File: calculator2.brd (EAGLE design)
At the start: 72.8 x 140 mm, 41 parts

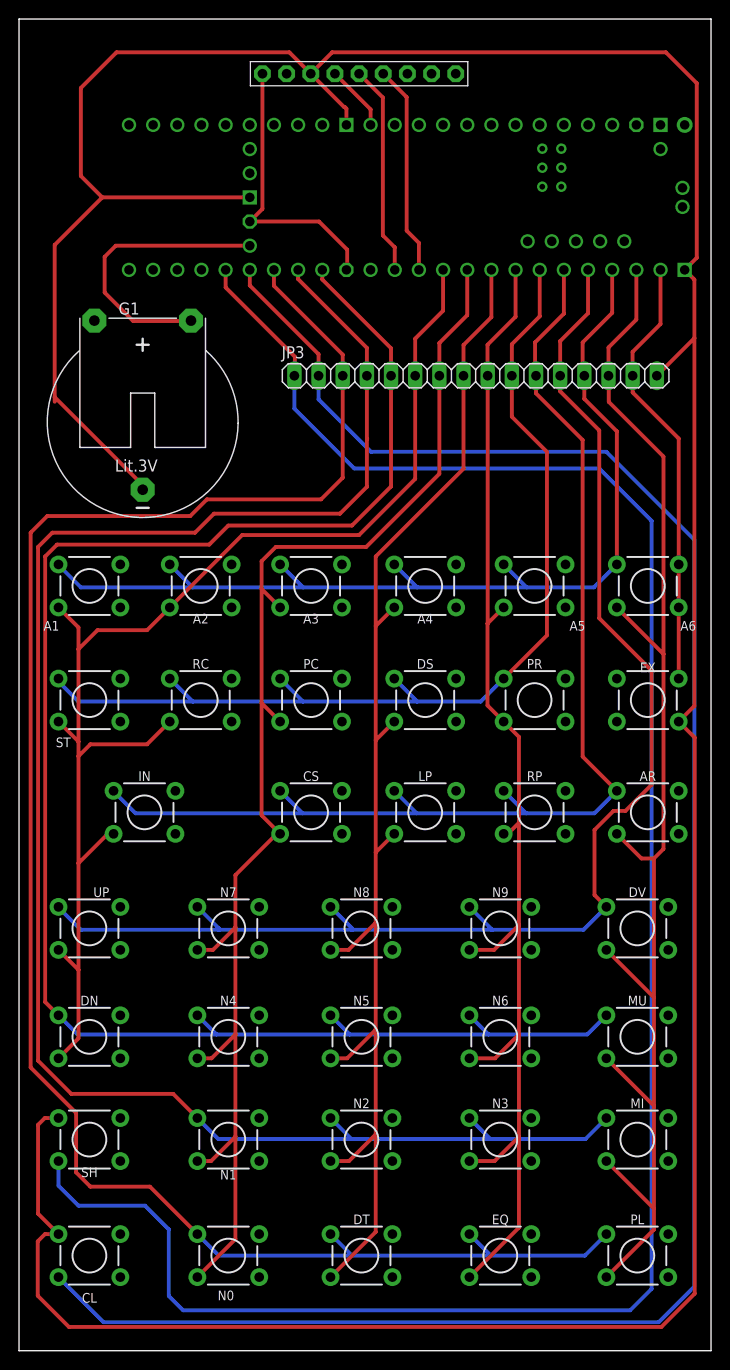
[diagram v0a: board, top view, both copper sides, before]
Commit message: Using 32 board
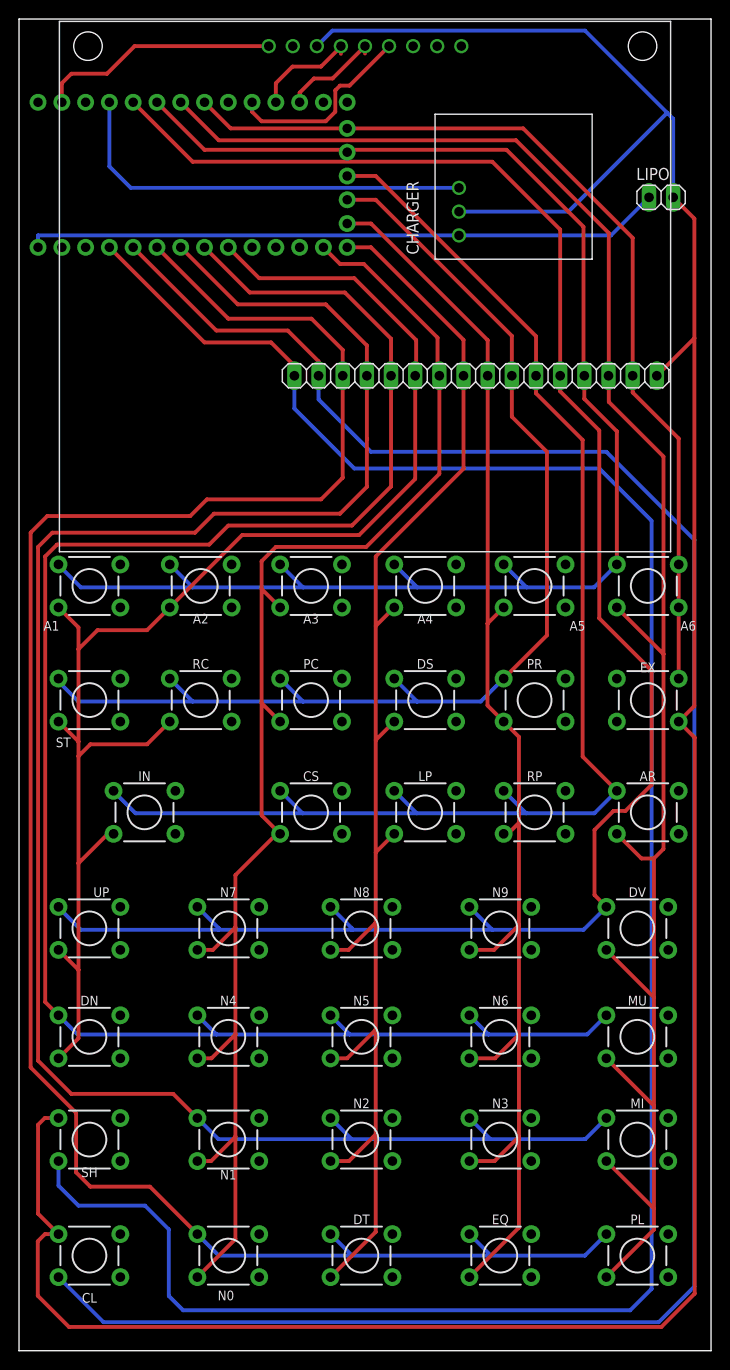
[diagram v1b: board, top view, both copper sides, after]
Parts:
- removed DISPLAY: (no value), adafruit:1X09-BIG
- removed G1: CR2032H, battery:CR2032H
- removed U$1: TEENSY41, teensy:TEENSY41
- added CHARGER: PROTRINKET, pwlib:PROTRINKET
- added CONTROLLER: IB32U4, pwlib:IB32U4
- added LIPO: (no value), pinhead:1X02
- added SHARPMEM: SHARPMEM, pwlib:SHARPMEM
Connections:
- removed net N$2: G1.+, U$1.VBAT
- removed net SCK: DISPLAY.4, U$1.13-SCK/LED
- new net N$1: CHARGER.BAT, CONTROLLER.BAT, LIPO.1
- new net SLCK: CONTROLLER.SCK, SHARPMEM.SLCK
- new net VHI: CHARGER.+5V, CONTROLLER.VHI
- net 3V3: now also CONTROLLER.3V3, SHARPMEM.VIN; no longer DISPLAY.1, U$1.3V3-1, U$1.3V3-2
- net C1: now also CONTROLLER.7; no longer U$1.9-OUT1C
- net C2: now also CONTROLLER.1; no longer U$1.8-TX2/IN2
- net C3: now also CONTROLLER.0; no longer U$1.7-RX2/OUT1A
- net C4: now also CONTROLLER.4; no longer U$1.6-OUT1D
- net C5: now also CONTROLLER.A2; no longer U$1.1-TX1/MISO1/CTX2
- net CL: now also CONTROLLER.12; no longer U$1.27-A13/SCK1
- net CS: now also CONTROLLER.A5, SHARPMEM.CS; no longer DISPLAY.6, U$1.10-CS\MQSR
- net EX: now also CONTROLLER.A3; no longer U$1.0-RX1/CS1/CRX2
- net GND: now also CHARGER.GND, LIPO.2, SHARPMEM.GND; no longer DISPLAY.3, G1.-, U$1.GND1, U$1.GND2, U$1.GND3
- net MOSI: now also CONTROLLER.MO, SHARPMEM.MOSI; no longer DISPLAY.5, U$1.11-MOSI/CTX1
- net R1: now also CONTROLLER.A1; no longer U$1.2-OUT2
- net R2: now also CONTROLLER.6; no longer U$1.5-IN2
- net R3: now also CONTROLLER.8; no longer U$1.4-BCLK2
- net R4: now also CONTROLLER.A0; no longer U$1.3-LRCLK2
- net R5: now also CONTROLLER.9; no longer U$1.24-A10/TX6/SCL2
- net R6: now also CONTROLLER.10; no longer U$1.25-A11/RX6/SDA2
- net R7: now also CONTROLLER.11; no longer U$1.26-A12/MOSI1
- net SH: now also CONTROLLER.13; no longer U$1.28-RX7
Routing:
- net GND: track 371.6 -> 294.5 mm
- net N$1: track 0.00 -> 67.1 mm
- net R1: track 108.1 -> 161.7 mm
- net R4: track 145.6 -> 199.1 mm
- net C5: track 145.1 -> 198.5 mm
- net EX: track 46.9 -> 99.3 mm
- net VHI: track 0.00 -> 44.4 mm
- net N$2: track 29.8 -> 0.00 mm
- net R3: track 124.5 -> 143.2 mm
- net C1: track 137.2 -> 152.7 mm
- net R2: track 106.8 -> 121.9 mm
- net R5: track 181.8 -> 195.1 mm
- net R6: track 187.4 -> 200.3 mm
- net R7: track 196.0 -> 208.6 mm
- net CL: track 211.1 -> 222.9 mm
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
